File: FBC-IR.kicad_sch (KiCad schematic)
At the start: 18 parts, among them J1 IR LED, J2 IR LED, J3 IR LED, J4 IR LED, Q1 BC850W, Q2 BC850W

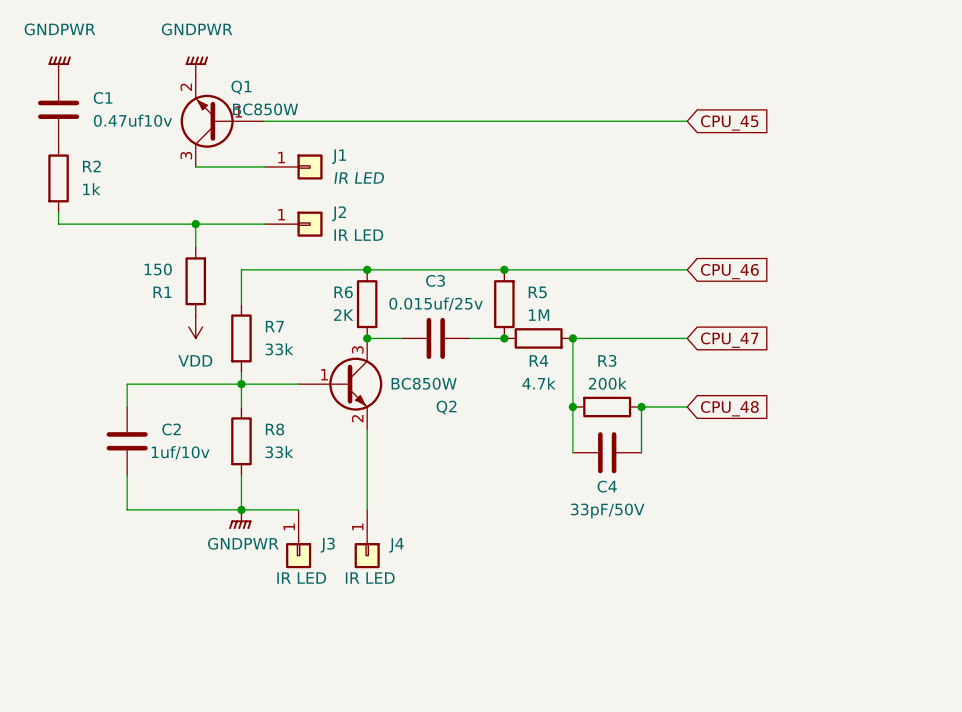
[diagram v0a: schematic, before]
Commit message: Add files via upload
Added CPU connection footprints and LED solder pad footprints
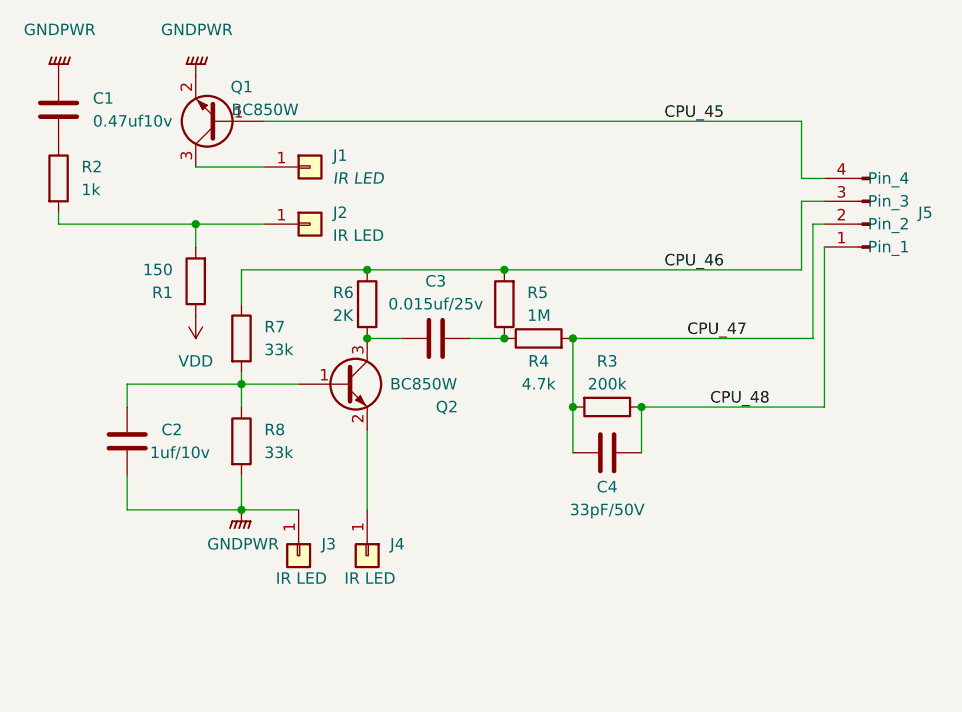
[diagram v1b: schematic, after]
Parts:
- added J5: Conn_01x04_Pin, Customs:CPU_connector, symbol Connector:Conn_01x04_Pin
- J1: footprint customs:LED_pads -> Customs:LED_pad
- J2, J3, J4: footprint Connector_Wire:SolderWirePad_1x01_SMD_1x2mm -> Customs:LED_pad
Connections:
- net CPU_45: now also J5.4 (Pin_4)
- net CPU_46: now also J5.3 (Pin_3)
- net CPU_47: now also J5.2 (Pin_2)
- net CPU_48: now also J5.1 (Pin_1)
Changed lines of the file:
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@@
+	(wire
+		(pts
+			(xy 129.54 68.58) (xy 130.81 68.58)
+		)
+		(stroke
+			(width 0)
+			(type default)
+		)
+	)
 	(wire
 		(pts
@@
 	(wire
 		(pts
+			(xy 130.81 88.9) (xy 130.81 71.12)
+		)
+		(stroke
+			(width 0)
+			(type default)
+		)
+	)
+	(wire
+		(pts
 			(xy 53.34 86.36) (xy 66.04 86.36)
 		)
@@
 	(wire
 		(pts
+			(xy 128.27 73.66) (xy 128.27 66.04)
+		)
+		(stroke
+			(width 0)
+			(type default)
+		)
+	)
+	(wire
+		(pts
 			(xy 80.01 91.44) (xy 80.01 100.33)
 		)
@@
 	(wire
 		(pts
+			(xy 128.27 66.04) (xy 130.81 66.04)
+		)
+		(stroke
+			(width 0)
+			(type default)
+		)
+	)
+	(wire
+		(pts
 			(xy 53.34 88.9) (xy 53.34 86.36)
 		)
@@
 	(wire
 		(pts
-			(xy 68.58 57.15) (xy 115.57 57.15)
+			(xy 68.58 57.15) (xy 128.27 57.15)
 		)
 		(stroke
@@
 	(wire
 		(pts
-			(xy 102.87 81.28) (xy 115.57 81.28)
-		)
-		(stroke
-			(width 0)
-			(type default)
-		)
-	)
-	(wire
-		(pts
-			(xy 95.25 73.66) (xy 115.57 73.66)
+			(xy 102.87 81.28) (xy 129.54 81.28)
+		)
+		(stroke
+			(width 0)
+			(type default)
+		)
+	)
+	(wire
+		(pts
+			(xy 95.25 73.66) (xy 128.27 73.66)
 		)
 		(stroke
@@
 	(wire
 		(pts
-			(xy 110.49 88.9) (xy 115.57 88.9)
+			(xy 128.27 57.15) (xy 128.27 63.5)
+		)
+		(stroke
+			(width 0)
+			(type default)
+		)
+	)
+	(wire
+		(pts
+			(xy 129.54 81.28) (xy 129.54 68.58)
+		)
+		(stroke
+			(width 0)
+			(type default)
+		)
+	)
+	(wire
+		(pts
+			(xy 110.49 88.9) (xy 130.81 88.9)
 		)
 		(stroke
@@
 	(wire
 		(pts
+			(xy 128.27 63.5) (xy 130.81 63.5)
+		)
+		(stroke
+			(width 0)
+			(type default)
+		)
+	)
+	(wire
+		(pts
 			(xy 66.04 73.66) (xy 66.04 77.47)
 		)
@@
 		)
 	)
-	(global_label "CPU_45"
-		(shape input)
-		(at 115.57 57.15 0)
+	(label "CPU_46"
+		(at 113.03 73.66 0)
 		(fields_autoplaced yes)
 		(effects
@@
 				(size 1.27 1.27)
 			)
-			(justify left)
-		)
-		(property "Intersheetrefs" "${INTERSHEET_REFS}"
-			(at 125.2402 57.0706 0)
-			(effects
-				(font
-					(size 1.27 1.27)
-				)
-				(justify left)
-				(hide yes)
-			)
-		)
-	)
-	(global_label "CPU_48"
-		(shape input)
-		(at 115.57 88.9 0)
-		(fields_autoplaced yes)
-		(effects
-			(font
-				(size 1.27 1.27)
-			)
-			(justify left)
-		)
-		(property "Intersheetrefs" "${INTERSHEET_REFS}"
-			(at 125.2402 88.8206 0)
-			(effects
-				(font
-					(size 1.27 1.27)
-				)
-				(justify left)
-				(hide yes)
-			)
-		)
-	)
-	(global_label "CPU_46"
-		(shape input)
-		(at 115.57 73.66 0)
-		(fields_autoplaced yes)
-		(effects
-			(font
-				(size 1.27 1.27)
-			)
-			(justify left)
-		)
-		(property "Intersheetrefs" "${INTERSHEET_REFS}"
-			(at 125.2402 73.5806 0)
-			(effects
-				(font
-					(size 1.27 1.27)
-				)
-				(justify left)
-				(hide yes)
-			)
-		)
-	)
-	(global_label "CPU_47"
-		(shape input)
+			(justify left bottom)
+		)
+	)
+	(label "CPU_47"
 		(at 115.57 81.28 0)
 		(fields_autoplaced yes)
@@
 				(size 1.27 1.27)
 			)
-			(justify left)
-		)
-		(property "Intersheetrefs" "${INTERSHEET_REFS}"
-			(at 125.2402 81.2006 0)
-			(effects
-				(font
-					(size 1.27 1.27)
-				)
-				(justify left)
-				(hide yes)
+			(justify left bottom)
+		)
+	)
+	(label "CPU_48"
+		(at 118.11 88.9 0)
+		(fields_autoplaced yes)
+		(effects
+			(font
+				(size 1.27 1.27)
+			)
+			(justify left bottom)
+		)
+	)
+	(label "CPU_45"
+		(at 113.03 57.15 0)
+		(fields_autoplaced yes)
+		(effects
+			(font
+				(size 1.27 1.27)
+			)
+			(justify left bottom)
+		)
+	)
+	(symbol
+		(lib_id "Connector:Conn_01x04_Pin")
+		(at 135.89 68.58 180)
+		(unit 1)
+		(exclude_from_sim no)
+		(in_bom yes)
+		(on_board yes)
+		(dnp no)
+		(property "Reference" "J5"
+			(at 141.224 67.31 0)
+			(effects
+				(font
+					(size 1.27 1.27)
+				)
+				(justify right)
+			)
+		)
+		(property "Value" "Conn_01x04_Pin"
+			(at 137.16 68.5799 0)
+			(effects
+				(font
+					(size 1.27 1.27)
+				)
+				(justify right)
+				(hide yes)
+			)
+		)
+		(property "Footprint" "Customs:CPU_connector"
+			(at 135.89 68.58 0)
+			(effects
+				(font
+					(size 1.27 1.27)
+				)
+				(hide yes)
+			)
+		)
+		(property "Datasheet" "~"
+			(at 135.89 68.58 0)
+			(effects
+				(font
+					(size 1.27 1.27)
+				)
+				(hide yes)
+			)
+		)
+		(property "Description" "Generic connector, single row, 01x04, script generated"
+			(at 135.89 68.58 0)
+			(effects
+				(font
+					(size 1.27 1.27)
+				)
+				(hide yes)
+			)
+		)
+		(pin "4"
+		)
+		(pin "3"
+		)
+		(pin "1"
+		)
+		(pin "2"
+		)
+		(instances
+			(project "FBC-IR"
+				(path "/7234510c-a57b-4449-9b96-152fea1cbda0"
+					(reference "J5")
+					(unit 1)
+				)
 			)
 		)
@@
 			)
 		)
-		(property "Footprint" "Connector_Wire:SolderWirePad_1x01_SMD_1x2mm"
+		(property "Footprint" "Customs:LED_pad"
 			(at 73.66 68.58 0)
 			(effects
@@
 			)
 		)
-		(property "Footprint" "Connector_Wire:SolderWirePad_1x01_SMD_1x2mm"
+		(property "Footprint" "Customs:LED_pad"
 			(at 80.01 105.41 0)
 			(effects
@@
 			)
 		)
-		(property "Footprint" "Connector_Wire:SolderWirePad_1x01_SMD_1x2mm"
+		(property "Footprint" "Customs:LED_pad"
 			(at 72.39 105.41 0)
 			(effects
@@
 			)
 		)
-		(property "Footprint" "customs:LED_pads"
+		(property "Footprint" "Customs:LED_pad"
 			(at 73.66 62.23 0)
 			(effects

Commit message: Add files via upload
Fixed CPU connectors causing DRC error. Replaced LED pads with a 1x4 footprint. Fixed Q1 and Q2 footprints not matching prior footprint due to kicad 8.0 upgrade
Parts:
- removed J1, J2, J3, J4: IR LED, Customs:LED_pad, symbol Connector_Generic:Conn_01x01
- added J6: Conn_01x04_Pin, Customs:LED_pad, symbol Connector:Conn_01x04_Pin
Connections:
- net GNDPWR: now also J6.2 (Pin_2)
- net IR_2: now reaches R1.2, R2.2
- net IR_2: now also J6.4 (Pin_4)
- net IR_1: now reaches Q1.3 (C)
- net IR_1: now also J6.3 (Pin_3)
- net PT_2: now reaches Q2.2 (E)
- net PT_2: now also J6.1 (Pin_1)
